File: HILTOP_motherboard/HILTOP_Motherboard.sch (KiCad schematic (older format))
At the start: 119 parts, among them J1 Conn_02x10_Odd_Even, J10 HDMI, J11 DISP_PWR, J12 DISPLAY_PORT, J14 PROG_PWR2, J15 PROG_PWR1, J16 SOFT_START_PWR, J17 PWR_LED, J18 USB_B, J19 Micro_SD_Card, J2 ATX_MOLEX_02X12, J20 CAMERA_PORT, J21 EXT_FAN, J24 Conn_02x10_Odd_Even, J3 SATA, J4 USB_A_DOUBLE, J5 USB Front Panel, J6 Conn_02x05_Odd_Even, J7 Conn_02x08_Odd_Even, J8 EXT_TEMP_MON, J9 RJ45-TRANS_SI-61001-F, Q5 ZXMN6A07F, U1 LM2664, U25 STM6719SFWB6F

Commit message: Schematics complete - 1st draft
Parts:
- removed C50: 3.3uF, Capacitor_SMD:C_0805_2012Metric, symbol C
- removed C74, C75: 100nF, Capacitor_SMD:C_0603_1608Metric, symbol C
- removed C77: 100nF, Capacitor_SMD:C_0201_0603Metric, symbol C
- removed EXP2, EXP3: CONN_02X20, Connector_PinHeader_2.54mm:PinHeader_2x20_P2.54mm_Vertical, symbol CONN_02X20
- removed J1, J24: Conn_02x10_Odd_Even, Connector_PinHeader_2.54mm:PinHeader_2x10_P2.54mm_Vertical, symbol Conn_02x10_Odd_Even
- removed Q5: ZXMN6A07F, Package_TO_SOT_SMD:SOT-23, symbol Q_NMOS_GSD
- removed R10, R11, R19, R8, R82, R9: DNF, Resistor_SMD:R_0603_1608Metric, symbol R
- removed R13, R15, R26, R29: 4K7, Resistor_SMD:R_0603_1608Metric, symbol R
- removed R18: 0R, Resistor_SMD:R_0603_1608Metric, symbol R
- removed R24, R25: 470R, Resistor_SMD:R_0603_1608Metric, symbol R
- removed R28: 10K, Resistor_SMD:R_0603_1608Metric, symbol R
- removed U1: LM2664, Package_TO_SOT_SMD:SOT-23-6, symbol LM2664
- added C50, C75, C77: 100nF, Capacitor_SMD:C_0603_1608Metric, symbol device:C
- added C74: 1uF, Capacitor_SMD:C_0805_2012Metric, symbol device:C
- added EXP2, EXP3: CONN_02X20, Connector_PinHeader_2.54mm:PinHeader_2x20_P2.54mm_Vertical, symbol HILTOP_Motherboard-rescue:CONN_02X20
- added F1: PPTC 2A, 3.8A, 32V, Fuse:Fuse_Bourns_MF-RHT200, symbol device:Polyfuse
- added F2, F3: Polyfuse, Fuse:Fuse_1206_3216Metric, symbol device:Polyfuse
- added J1: BACKPLANE_PWR, Connector_Molex:Molex_Mini-Fit_Jr_5566-08A_2x04_P4.20mm_Vertical, symbol Connector:Conn_02x04_Top_Bottom
- added J22: BACKPLANE_LV_PWR, Connector_Molex:Molex_Mini-Fit_Jr_5566-04A_2x02_P4.20mm_Vertical, symbol Connector:Conn_02x02_Top_Bottom
- added J23: EXT_FAN, Connector_Molex:Molex_KK-254_AE-6410-04A_1x04_P2.54mm_Vertical, symbol Connector:Conn_01x04
- added R10, R11, R18, R19: 0R, Resistor_SMD:R_0603_1608Metric, symbol device:R
- added R24: DNF, Resistor_SMD:R_0603_1608Metric, symbol device:R
- added R25: 10K, Resistor_SMD:R_0603_1608Metric, symbol device:R
- added R8: 590R, Resistor_SMD:R_1206_3216Metric, symbol device:R
- added R9: 120R, Resistor_SMD:R_0603_1608Metric, symbol device:R
- added TP15, TP16: Test_Point, TestPoint:TestPoint_THTPad_D1.0mm_Drill0.5mm, symbol Connector:Test_Point
- added U1: LM337BD2TG, Package_TO_SOT_SMD:TO-263-2, symbol regul:LM337_TO263
- added U39: MCP23017, Package_SO:SOIC-28W_7.5x17.9mm_P1.27mm, symbol microchip:MCP23S17
- C1, C12, C121, C14, C15, C17, C19, C20, C22, C24, C25, C26, C27, C5, C51, C53, C55, C59, C71, C72, C73, C8: symbol C -> device:C
- C10, C11, C119, C120, C13, C16, C18, C2, C3, C4, C6, C7, C9: symbol CP -> device:CP
- D1: symbol LED -> device:LED
- EXP1: symbol CONN_02X20 -> HILTOP_Motherboard-rescue:CONN_02X20
- J10: symbol HDMI -> Devtank:HDMI
- J11: symbol CONN_01X05 -> HILTOP_Motherboard-rescue:CONN_01X05
- J12, J20: symbol CONN_01X15 -> HILTOP_Motherboard-rescue:CONN_01X15
- J14: value PROG_PWR2 -> VADJ_B; symbol CONN_01X02 -> Connector:Conn_01x02
- J15: value PROG_PWR1 -> VADJ_A; symbol CONN_01X02 -> Connector:Conn_01x02
- J16, J17: symbol CONN_01X02 -> HILTOP_Motherboard-rescue:CONN_01X02
- J18: symbol USB_B -> Connector:USB_B
- J19: symbol Micro_SD_Card -> Connector:Micro_SD_Card
- J2: symbol ATX_MOLEX_02X12 -> Devtank:ATX_MOLEX_02X12
- J21: symbol Conn_01x04 -> Connector:Conn_01x04
- J3: symbol Conn_01x07 -> Connector:Conn_01x07
- J4: symbol USB_A_DOUBLE -> Devtank:USB_A_DOUBLE
- J5: symbol Conn_01x08 -> Connector:Conn_01x08
- J6: symbol Conn_02x05_Odd_Even -> Connector:Conn_02x05_Odd_Even
- J7: symbol Conn_02x08_Odd_Even -> Connector:Conn_02x08_Odd_Even
- J8: symbol Conn_01x03 -> Connector:Conn_01x03
- J9: symbol RJ45-TRANS_SI-61001-F -> Devtank:RJ45-TRANS_SI-61001-F
- L1, L2, L3, L8: symbol L_Core_Ferrite -> device:L_Core_Ferrite
- R1, R119, R12, R120, R121, R122, R124, R125, R14, R148, R149, R150, R151, R16, R17, R2, R22, R23, R3, R4, R5, R54, R56, R6, R7, R83, R85: symbol R -> device:R
- TP10, TP11, TP12, TP13, TP14, TP8, TP9: footprint TestPoint:TestPoint_THTPad_D1.5mm_Drill0.7mm -> TestPoint:TestPoint_THTPad_D1.0mm_Drill0.5mm; symbol TEST_1P -> HILTOP_Motherboard-rescue:TEST_1P
- U25: symbol STM6719SFWB6F -> Devtank:STM6719SFWB6F
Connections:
- net labels added: FAN_SENSE_1, FAN_SENSE_2, MCP23017_INTA, MCP23017_INTB, UART_CH1_CS, UART_CH1_IRQ, UART_CH2_CS, UART_CH2_IRQ
- net labels removed: CAN_DIN, CAN_DOUT, CAN_SCK, D1_MISO_N, D1_MISO_P, D1_MOSI_N, D1_MOSI_P, D2_MISO_N, D2_MISO_P, D2_MOSI_N, D2_MOSI_P, D3_MISO_N, D3_MISO_P, D3_MOSI_N, D3_MOSI_P, D4_MISO_N, D4_MISO_P, D4_MOSI_N, D4_MOSI_P, D5_MISO_N, D5_MISO_P, D5_MOSI_N, D5_MOSI_P, D6_MISO_N, D6_MISO_P, D6_MOSI_N, D6_MOSI_P, FAN_SENSE, FP_GPIO_1, FP_GPIO_10, FP_GPIO_11, FP_GPIO_12, FP_GPIO_13, FP_GPIO_14, FP_GPIO_15, FP_GPIO_16, FP_GPIO_17, FP_GPIO_18, FP_GPIO_19, FP_GPIO_2, FP_GPIO_20, FP_GPIO_21, FP_GPIO_22, FP_GPIO_23, FP_GPIO_24, FP_GPIO_25, FP_GPIO_26, FP_GPIO_27, FP_GPIO_28, FP_GPIO_29, FP_GPIO_3, FP_GPIO_30, FP_GPIO_31, FP_GPIO_32, FP_GPIO_33, FP_GPIO_4, FP_GPIO_5, FP_GPIO_6, FP_GPIO_7, FP_GPIO_8, FP_GPIO_9, PR_GPIO10, PR_GPIO11, PR_GPIO12, PR_GPIO13, PR_GPIO14, PR_GPIO15, PR_GPIO16, PR_GPIO17, PR_GPIO18, PR_GPIO19, PR_GPIO20, PR_GPIO21, PR_GPIO9, PSU_ALERT, PWR_ENABLE, SYS_CLK_N, SYS_CLK_P
- wire segments 881 -> 996
- no-connect marks 1 -> 0
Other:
- moved on the sheet: EXP1, TP11

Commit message: BOM nearly complete!
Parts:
- removed TP15, TP16: Test_Point, TestPoint:TestPoint_THTPad_D1.0mm_Drill0.5mm, symbol Connector:Test_Point
- added D34, D35, D93, D94, D95, D96: BAV99, Package_TO_SOT_SMD:SOT-23, symbol Diode:BAV99
- added J26: Conn_02x06_Odd_Even, Connector_IDC:IDC-Header_2x06_P2.54mm_Vertical, symbol Connector:Conn_02x06_Odd_Even
- added R245, R246, R247, R248, R249: 220R, Resistor_SMD:R_0402_1005Metric, symbol device:R
- added TP15, TP16, TP17, TP18, TP19, TP20, TP21, TP22, TP23, TP24, TP25, TP26, TP27, TP28, TP29, TP30, TP31, TP32, TP33, TP34, TP35, TP36, TP37, TP38, TP39, TP40, TP41, TP42, TP43, TP44, TP45, TP46, TP47, TP48, TP49, TP50, TP51, TP52, TP53, TP54, TP55, TP56, TP57, TP58, TP59, TP60, TP61, TP62, TP63, TP64, TP65, TP66, TP67, TP68, TP69, TP70, TP71, TP72, TP73, TP74, TP75, TP76, TP77, TP78, TP79, TP80, TP81, TP82, TP83, TP84, TP85, TP86, TP87, TP88, TP89, TP90, TP91, TP92, TP93, TP94: TP, TestPoint:TestPoint_THTPad_D1.0mm_Drill0.5mm, symbol HILTOP_Motherboard-rescue:TEST_1P
- D1: value Green_LED -> GRN; footprint LED_SMD:LED_0603_1608Metric -> LED_SMD:LED_0402_1005Metric; Devtank 110-002 -> 110-005
- EXP1, EXP2, EXP3: footprint Connector_PinHeader_2.54mm:PinHeader_2x20_P2.54mm_Vertical -> Connector_IDC:IDC-Header_2x20_P2.54mm_Vertical
- F1: value PPTC 2A, 3.8A, 32V -> PPTC 3.8A
- F2, F3: Devtank (none) -> 190-002
- J12, J20: footprint Devtank_PCB_Lib:DSI_SFW15R-2STE1LF -> Devtank_PCB_Lib:DSI_FCC15W_VERT; Devtank 702-002 -> 702-003
- R54: value DNF -> 220R; footprint Resistor_SMD:R_0603_1608Metric -> Resistor_SMD:R_0402_1005Metric; Devtank (none) -> 101-049
- U39: Devtank (none) -> 123-007
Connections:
- net labels added: EXT_GPIO1, EXT_GPIO2, EXT_GPIO3, EXT_GPIO4, EXT_GPIO5, EXT_GPIO6
- net labels removed: FPGA_USB_N, FPGA_USB_P
- wire segments 996 -> 1084
- no-connect marks 0 -> 8
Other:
- moved on the sheet: C15, C20, C77, J7, R10, R11, R18, R19, R24, U39

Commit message: nearly finished placing all parts!
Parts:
- removed C53, C55: 100nF, Capacitor_SMD:C_0201_0603Metric, symbol device:C
- removed C59, C71, C72, C73: 100nF, Capacitor_SMD:C_0603_1608Metric, symbol device:C
- removed EXP3: CONN_02X20, Connector_IDC:IDC-Header_2x20_P2.54mm_Vertical, symbol HILTOP_Motherboard-rescue:CONN_02X20
- J1: Devtank (none) -> 709-005
- J18: Devtank (none) -> 703-002
- J21, J23: Devtank (none) -> 710-013
- J22: Devtank (none) -> 709-006
- J26: value Conn_02x06_Odd_Even -> IO_EXP; Devtank (none) -> 710-002
- J5: value USB Front Panel -> USB FRONT PANEL
- J6: value Conn_02x05_Odd_Even -> CAN; Devtank (none) -> 714-002
- J7: value Conn_02x08_Odd_Even -> RS485; Devtank (none) -> 714-004
- J8: Devtank (none) -> 710-014
- U39: footprint Package_SO:SOIC-28W_7.5x17.9mm_P1.27mm -> Package_SO:SSOP-28_5.3x10.2mm_P0.65mm
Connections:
- net CAN1_INT0 is gone; now on net GND: TP36.1
- net CAN1_INT1 is gone; now on net GND: TP37.1
- net CAN2_INT0 is gone; now on net GND: TP41.1
- net CAN2_INT1 is gone; now on net GND: TP42.1
- net CAN1_INT: no longer TP35.1
- net CAN2_INT: no longer TP40.1
- net GND: now also TP35.1, TP40.1; no longer C15.2, C20.2
- net GND_ISO3: now also C15.2
- net GND_ISO4: now also C20.2
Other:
- note removed: "EACH EXP. PORT CONTAINS:\n+12V, +3.3V, +5V, -5V\nSystem Clock\nSystem PWM\n8 x GPIO Processor Pins\n11 x GPIO FPGA Pins\n"
- moved on the sheet: EXP1, EXP2

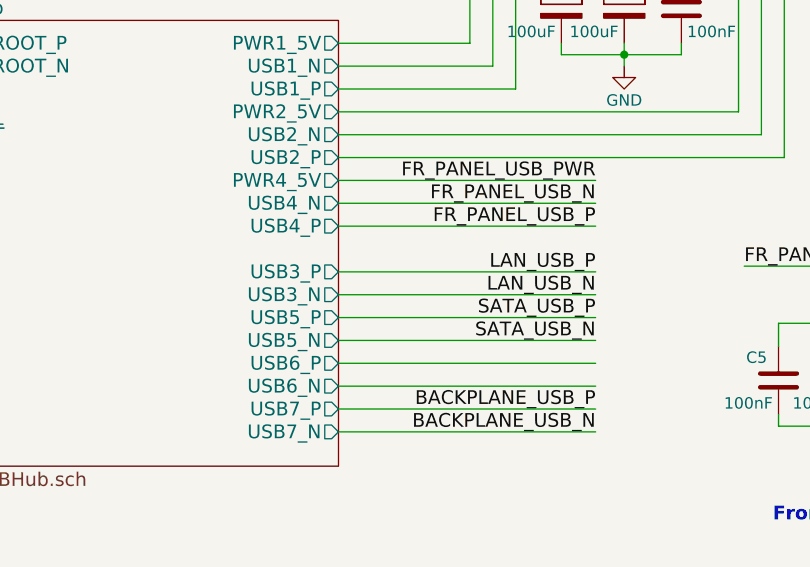
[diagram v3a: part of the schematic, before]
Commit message: All parts placed and backplane connector checked and locked
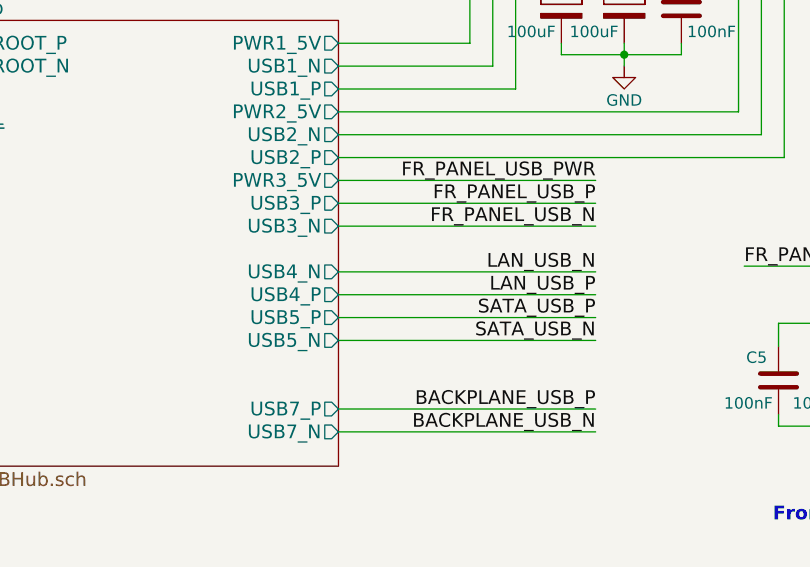
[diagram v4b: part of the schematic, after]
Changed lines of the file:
@@
 Sheet 1 12
 Title "HILTOP Motherboard"
-Date "26th January 2018"
+Date "2019-01-10"
 Rev "Issue 1"
 Comp "Devtank Ltd"
@@
 F4 "USB2_P" O R 4075 3300 60
 F5 "USB2_N" O R 4075 3200 60
-F6 "USB3_P" O R 4075 3800 60
-F7 "USB3_N" O R 4075 3900 60
-F8 "USB4_P" O R 4075 3600 60
-F9 "USB4_N" O R 4075 3500 60
+F6 "USB3_P" O R 4075 3500 60
+F7 "USB3_N" O R 4075 3600 60
+F8 "USB4_P" O R 4075 3900 60
+F9 "USB4_N" O R 4075 3800 60
 F10 "USB5_P" O R 4075 4000 60
 F11 "USB5_N" O R 4075 4100 60
-F12 "USB6_P" O R 4075 4200 60
-F13 "USB6_N" O R 4075 4300 60
-F14 "USB7_P" O R 4075 4400 60
-F15 "USB7_N" O R 4075 4500 60
-F16 "USB_ROOT_P" I L 2275 2800 60
-F17 "USB_ROOT_N" I L 2275 2900 60
-F18 "~RESET" I L 2275 3200 60
-F19 "PWR4_5V" O R 4075 3400 60
-F20 "PWR2_5V" O R 4075 3100 60
-F21 "PWR1_5V" O R 4075 2800 60
+F12 "USB7_P" O R 4075 4400 60
+F13 "USB7_N" O R 4075 4500 60
+F14 "USB_ROOT_P" I L 2275 2800 60
+F15 "USB_ROOT_N" I L 2275 2900 60
+F16 "~RESET" I L 2275 3200 60
+F17 "PWR3_5V" O R 4075 3400 60
+F18 "PWR2_5V" O R 4075 3100 60
+F19 "PWR1_5V" O R 4075 2800 60
 $EndSheet
 $Sheet
@@
 Text Label 1975 2900 2    60   ~ 0
 USB_ROOT_N
-Text Label 5200 3800 2    60   ~ 0
-LAN_USB_P
 Text Label 5200 3900 2    60   ~ 0
+LAN_USB_P
+Text Label 5200 3800 2    60   ~ 0
 LAN_USB_N
 Text Label 11550 1950 0    60   ~ 0
@@
 	1    0    0    -1
 $EndComp
-Text Label 5200 3600 2    60   ~ 0
-FR_PANEL_USB_P
 Text Label 5200 3500 2    60   ~ 0
+FR_PANEL_USB_P
+Text Label 5200 3600 2    60   ~ 0
 FR_PANEL_USB_N
 Text Label 5200 3400 2    60   ~ 0
@@
 	7500 3475 6575 3475
 Wire Wire Line
-	4075 3600 5200 3600
-Wire Wire Line
-	4075 3500 5200 3500
-Wire Wire Line
-	4075 3400 5200 3400
+	4075 3900 5200 3900
 Wire Wire Line
 	4075 3800 5200 3800
 Wire Wire Line
-	4075 3900 5200 3900
+	4075 3500 5200 3500
+Wire Wire Line
+	4075 3600 5200 3600
 Wire Wire Line
 	4075 4500 5200 4500
@@
 Wire Wire Line
 	11550 1950 12600 1950
-Wire Wire Line
-	4075 4300 5200 4300
-Wire Wire Line
-	4075 4200 5200 4200
 Connection ~ 4025 2000
 Wire Wire Line
@@
 Connection ~ 15325 14800
 $Comp
-L Devtank:GND_ISO3 #PWR?
+L Devtank:GND_ISO3 #PWR0283
 U 1 1 5DE9A8F7
 P 12550 9275
-F 0 "#PWR?" H 12550 9025 50  0001 C CNN
+F 0 "#PWR0283" H 12550 9025 50  0001 C CNN
 F 1 "GND_ISO3" H 12550 9125 50  0000 C CNN
 F 2 "" H 12550 9275 50  0000 C CNN
@@
 $EndComp
 $Comp
-L Devtank:GND_ISO4 #PWR?
+L Devtank:GND_ISO4 #PWR0286
 U 1 1 5DE9AAA2
 P 12975 9650
-F 0 "#PWR?" H 12975 9400 50  0001 C CNN
+F 0 "#PWR0286" H 12975 9400 50  0001 C CNN
 F 1 "GND_ISO4" H 12975 9500 50  0000 C CNN
 F 2 "" H 12975 9650 50  0000 C CNN
@@
 	1    0    0    -1
 $EndComp
+Wire Wire Line
+	4075 3400 5200 3400
 $EndSCHEMATC
